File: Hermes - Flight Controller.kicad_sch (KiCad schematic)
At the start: 1 part

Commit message: connector
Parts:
- added R?: (no value), symbol Device:R_Small
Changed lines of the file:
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@@
 (kicad_sch (version 20211123) (generator eeschema)
   (paper "A4")
+  (symbol (lib_id "Device:R_Small") (at 128.27 48.26 0) (unit 1)
+    (in_bom yes) (on_board yes) (fields_autoplaced)
+    (property "Reference" "R?" (id 0) (at 130.81 46.9899 0)
+      (effects (font (size 1.27 1.27)) (justify left))
+    )
+    (property "Value" "" (id 1) (at 130.81 49.5299 0)
+      (effects (font (size 1.27 1.27)) (justify left))
+    )
+    (property "Footprint" "" (id 2) (at 128.27 48.26 0)
+      (effects (font (size 1.27 1.27)) hide)
+    )
+    (property "Datasheet" "~" (id 3) (at 128.27 48.26 0)
+      (effects (font (size 1.27 1.27)) hide)
+    )
+    (pin "1")
+    (pin "2")
+  )
   (symbol (lib_id "Connector:USB_C_Receptacle_USB2.0") (at 88.9 54.61 0) (unit 1)
     (in_bom yes) (on_board yes) (fields_autoplaced)
@@
       (reference "J?") (unit 1) (value "USB_C_Receptacle_USB2.0") (footprint "")
     )
+    (path "/d8f1aa4a-2f21-4570-b6e4-a5df899c3581"
+      (reference "R?") (unit 1) (value "R_Small") (footprint "")
+    )
   )

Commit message: usbc implementation
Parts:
- added C? (x2): (no value), symbol Device:C_Small
- added FB?: (no value), symbol Device:FerriteBead_Small
- added R?: 5.1k, Resistor_SMD:R_0603_1608Metric_Pad0.98x0.95mm_HandSolder, symbol Device:R_Small
- added U?: USBLC6-2SC6, SnapEDA Library:SOT95P280X145-6N, symbol USBLC6-2SC6:USBLC6-2SC6
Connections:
- net at R?.1: now also J?.B5 (CC2)
- net GND: now reaches R?.2
- net GND: now also J?.A1 (GND), J?.A12 (GND), J?.B1 (GND), J?.B12 (GND), C?.2, C?.2, R?.2, U?.2
- net VBUS: now reaches J?.A4 (VBUS), J?.A9 (VBUS), J?.B4 (VBUS), J?.B9 (VBUS)
- net VBUS: now also C?.1, FB?.1, U?.5
- net at J?.A5 (CC1): now also R?.1
- net USB_CON_D+: now reaches J?.A6 (D+)
- net USB_CON_D+: now also J?.B6 (D+), U?.1
- net USB_CON_D-: now reaches J?.A7 (D-)
- net USB_CON_D-: now also J?.B7 (D-), U?.3
- new net: C?.1, FB?.2
- new net USB_D+: U?.6
- new net USB_D-: U?.4
- no-connect marks 0 -> 3
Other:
- moved on the sheet: R?

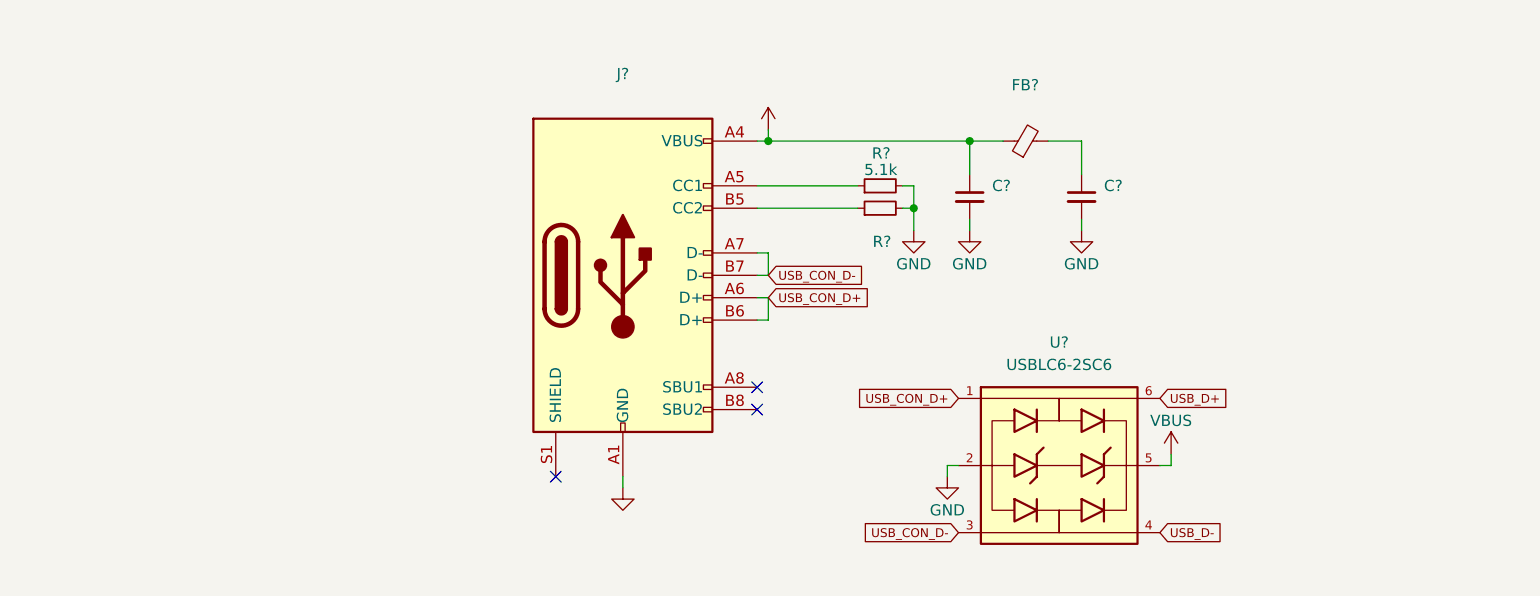
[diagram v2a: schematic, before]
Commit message: added battery charge circuit
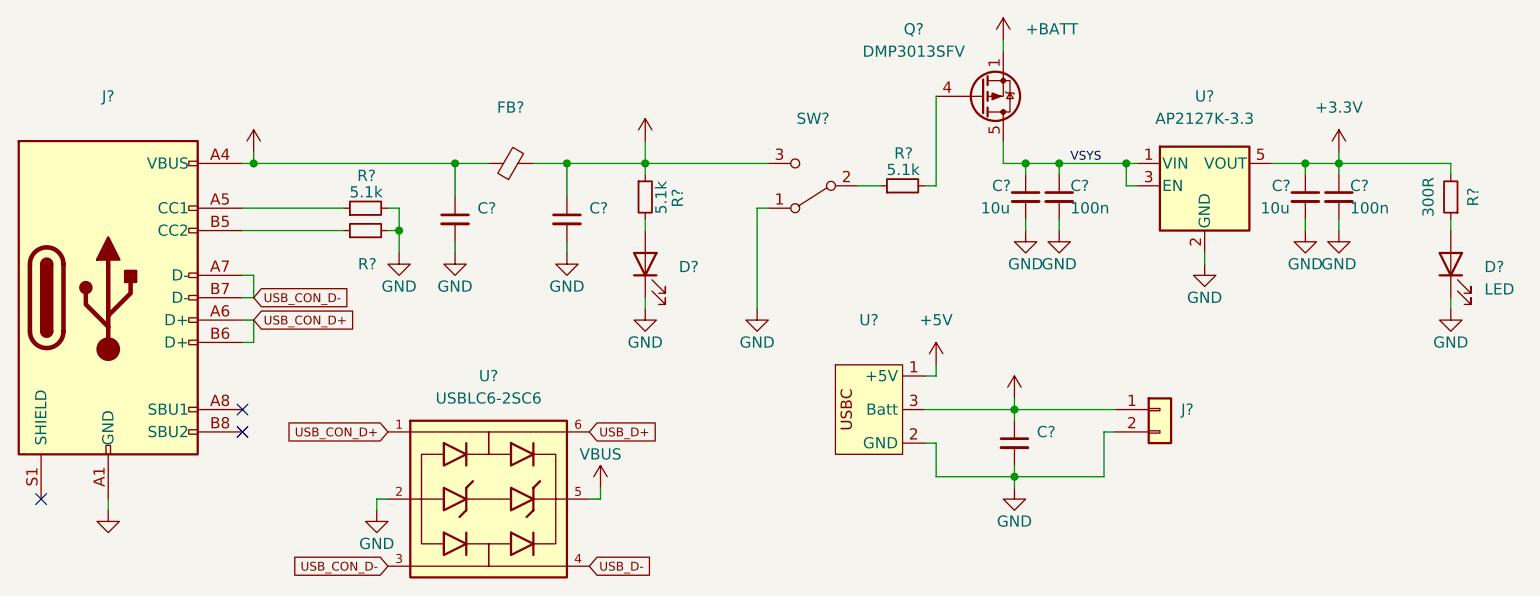
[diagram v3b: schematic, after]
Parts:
- added C?: (no value), symbol Device:C_Small
- added C? (x2): 10u, Resistor_SMD:R_0603_1608Metric_Pad0.98x0.95mm_HandSolder, symbol Device:C_Small
- added C? (x2): 100n, Resistor_SMD:R_0603_1608Metric_Pad0.98x0.95mm_HandSolder, symbol Device:C_Small
- added D?: LED, Resistor_SMD:R_0603_1608Metric_Pad0.98x0.95mm_HandSolder, symbol Device:LED
- added D?: (no value), symbol Device:LED
- added J?: (no value), symbol Connector_Generic:Conn_01x02
- added Q?: DMP3013SFV, Package_SON:Diodes_PowerDI3333-8, symbol Transistor_FET:DMP3013SFV
- added R? (x2): 5.1k, Resistor_SMD:R_0603_1608Metric_Pad0.98x0.95mm_HandSolder, symbol Device:R_Small
- added R?: 300R, Resistor_SMD:R_0603_1608Metric_Pad0.98x0.95mm_HandSolder, symbol Device:R_Small
- added SW?: (no value), symbol Switch:SW_SPDT
- added U?: AP2127K-3.3, Package_TO_SOT_SMD:SOT-23-5, symbol Regulator_Linear:AP2127K-3.3
- added U?: (no value), symbol usbc_batt:usbc_batt
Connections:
- net GND: now also C?.2, C?.2, C?.2, C?.2, C?.2, D?.1 (K), D?.1 (K), J?.2 (Pin_2), SW?.1 (A), U?.2 (GND), U?.2 (GND)
- net +5V: now reaches C?.1, FB?.2
- net +5V: now also R?.1, SW?.3 (C), U?.1 (+5V)
- new net: R?.1, SW?.2 (B)
- new net: D?.2 (A), R?.1
- new net: D?.2 (A), R?.2
- new net: Q?.4 (G), R?.2
- new net +3V3: C?.1, C?.1, R?.2, U?.5 (VOUT)
- new net +BATT: C?.1, J?.1 (Pin_1), Q?.1 (S), Q?.2 (S), Q?.3 (S), U?.3 (Batt)
- new net VSYS: C?.1, C?.1, Q?.5 (D), U?.1 (VIN), U?.3 (EN)
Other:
- moved on the sheet: C?, FB?, J?, R?, U?

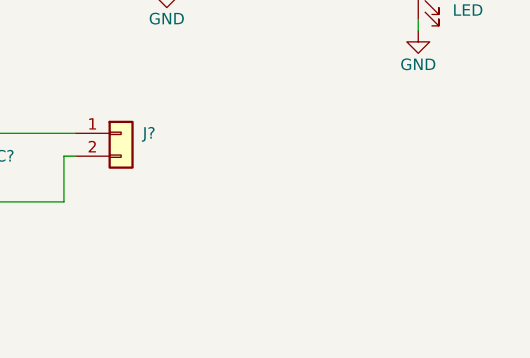
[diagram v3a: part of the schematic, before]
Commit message: opting for 2S battery config
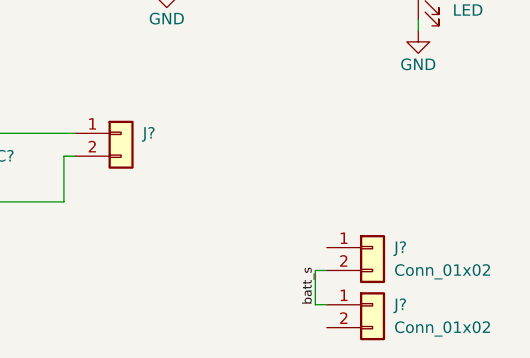
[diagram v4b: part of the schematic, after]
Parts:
- added J? (x2): Conn_01x02, symbol Connector_Generic:Conn_01x02
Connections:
- new net batt_s: J?.1 (Pin_1), J?.2 (Pin_2)
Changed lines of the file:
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@@
+    (stroke (width 0) (type default) (color 0 0 0 0))
+  )
+  (wire (pts (xy 172.72 85.09) (xy 171.45 85.09))
     (stroke (width 0) (type default) (color 0 0 0 0))
   )
@@
     (stroke (width 0) (type default) (color 0 0 0 0))
   )
+  (wire (pts (xy 171.45 85.09) (xy 171.45 88.9))
+    (stroke (width 0) (type default) (color 0 0 0 0))
+  )
   (wire (pts (xy 133.35 76.2) (xy 133.35 77.47))
     (stroke (width 0) (type default) (color 0 0 0 0))
@@
     (stroke (width 0) (type default) (color 0 0 0 0))
   )
+  (wire (pts (xy 171.45 88.9) (xy 172.72 88.9))
+    (stroke (width 0) (type default) (color 0 0 0 0))
+  )
   (label "VSYS" (at 139.7 41.91 0)
+    (effects (font (size 1 1)) (justify left bottom))
+  )
+  (label "batt_s" (at 171.45 88.9 90)
     (effects (font (size 1 1)) (justify left bottom))
   )
@@
     )
     (property "Datasheet" "~" (id 3) (at 182.88 45.72 0)
+      (effects (font (size 1.27 1.27)) hide)
+    )
+    (pin "1")
+    (pin "2")
+  )
+  (symbol (lib_id "Connector_Generic:Conn_01x02") (at 177.8 82.55 0) (unit 1)
+    (in_bom yes) (on_board yes) (fields_autoplaced)
+    (property "Reference" "J?" (id 0) (at 180.2029 82.5499 0)
+      (effects (font (size 1.27 1.27)) (justify left))
+    )
+    (property "Value" "Conn_01x02" (id 1) (at 180.2029 85.0899 0)
+      (effects (font (size 1.27 1.27)) (justify left))
+    )
+    (property "Footprint" "" (id 2) (at 177.8 82.55 0)
+      (effects (font (size 1.27 1.27)) hide)
+    )
+    (property "Datasheet" "~" (id 3) (at 177.8 82.55 0)
       (effects (font (size 1.27 1.27)) hide)
     )
@@
     (pin "2")
   )
+  (symbol (lib_id "Connector_Generic:Conn_01x02") (at 177.8 88.9 0) (unit 1)
+    (in_bom yes) (on_board yes) (fields_autoplaced)
+    (property "Reference" "J?" (id 0) (at 180.2029 88.8999 0)
+      (effects (font (size 1.27 1.27)) (justify left))
+    )
+    (property "Value" "Conn_01x02" (id 1) (at 180.2029 91.4399 0)
+      (effects (font (size 1.27 1.27)) (justify left))
+    )
+    (property "Footprint" "" (id 2) (at 177.8 88.9 0)
+      (effects (font (size 1.27 1.27)) hide)
+    )
+    (property "Datasheet" "~" (id 3) (at 177.8 88.9 0)
+      (effects (font (size 1.27 1.27)) hide)
+    )
+    (pin "1")
+    (pin "2")
+  )
   (sheet_instances
     (path "/" (page "1"))
@@
       (reference "J?") (unit 1) (value "Conn_01x02") (footprint "")
     )
+    (path "/bf5d4925-6bbb-4b21-ad5f-088d9d96ac60"
+      (reference "J?") (unit 1) (value "Conn_01x02") (footprint "")
+    )
     (path "/f12d2856-5cdd-423a-969e-209ea0a827b0"
       (reference "J?") (unit 1) (value "USB_C_Receptacle_USB2.0") (footprint "")
     )
+    (path "/fa5a923f-23c4-47c4-bacb-24bf6763083d"
+      (reference "J?") (unit 1) (value "Conn_01x02") (footprint "")
+    )
     (path "/d35736f0-de68-454d-9fb0-1a81541e123d"

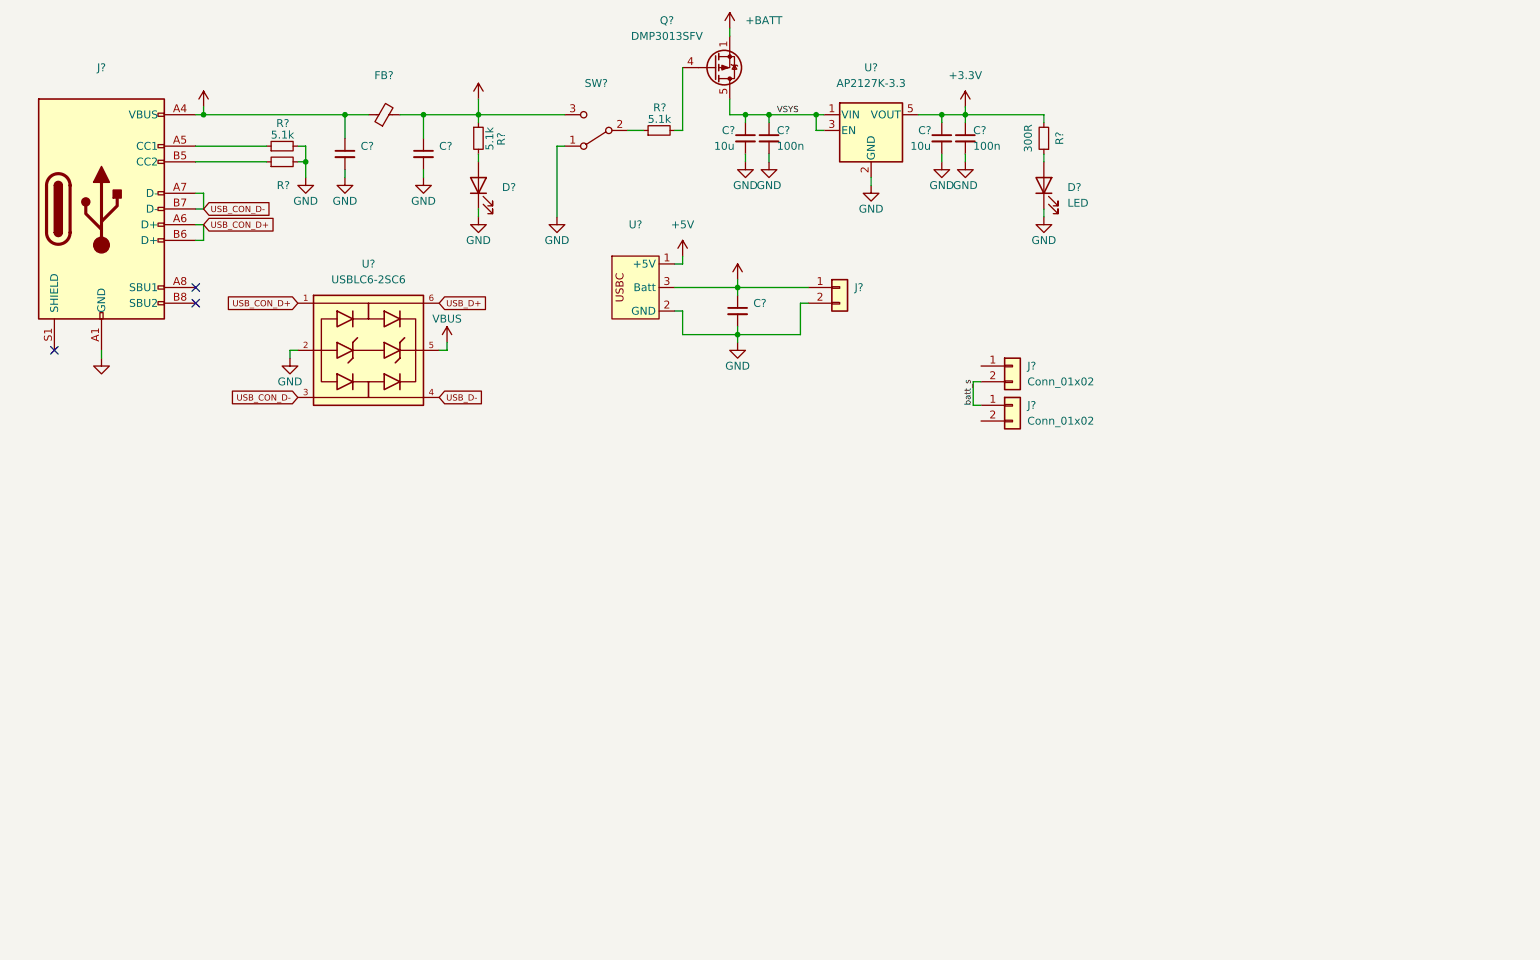
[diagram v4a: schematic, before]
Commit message: added pmic
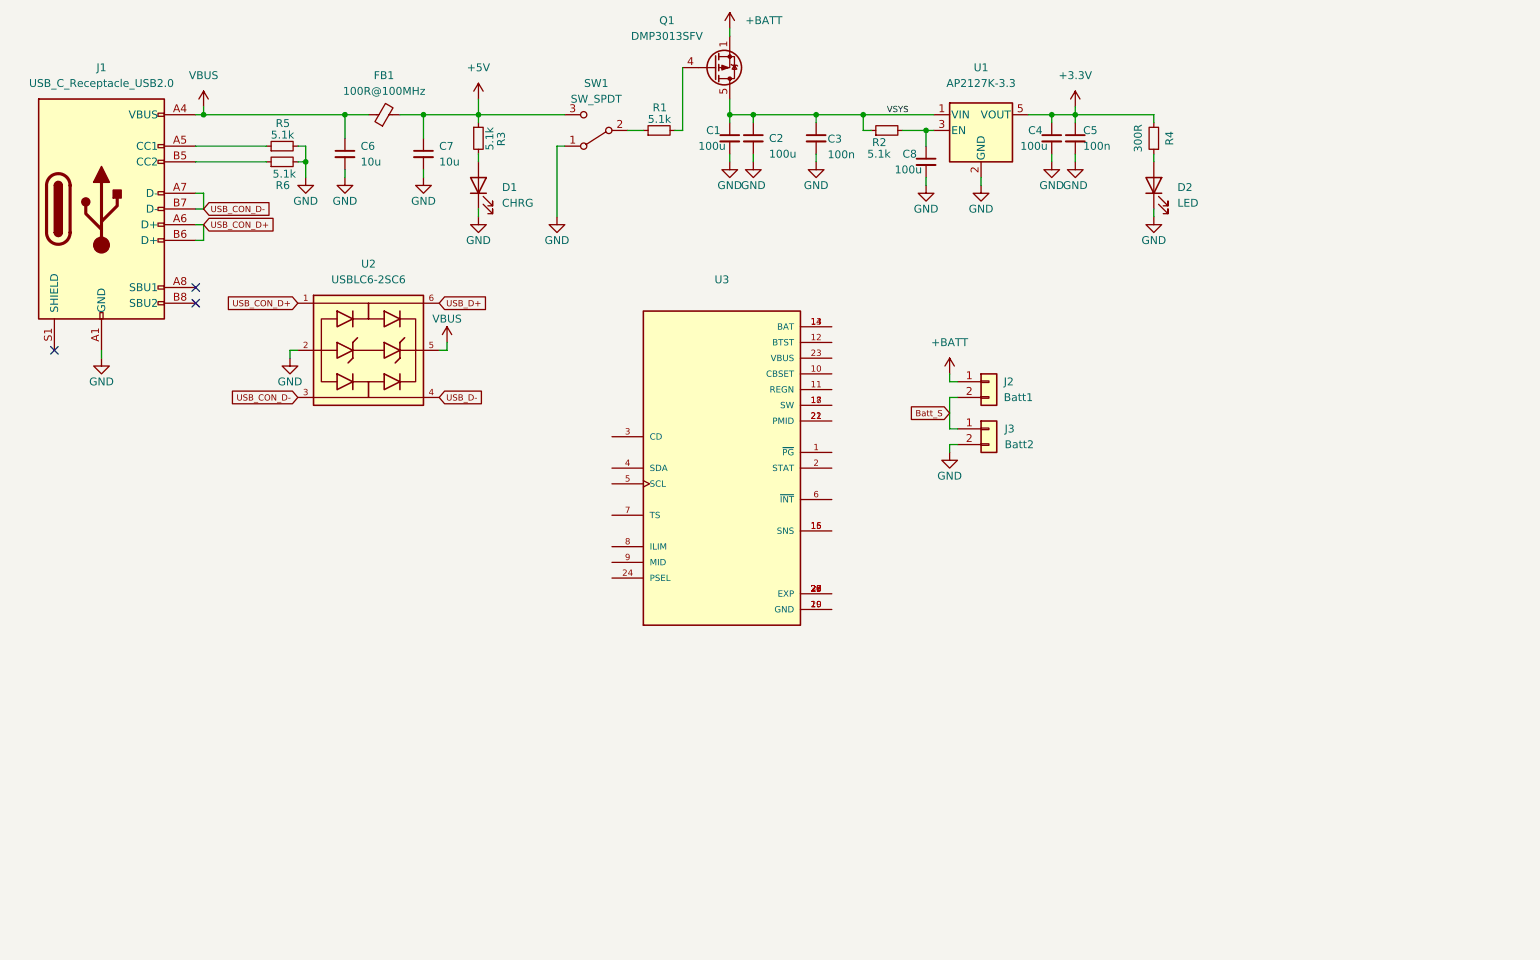
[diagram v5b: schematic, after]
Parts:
- removed C?: (no value), symbol Device:C_Small
- removed J?: (no value), symbol Connector_Generic:Conn_01x02
- removed U?: (no value), symbol usbc_batt:usbc_batt
- added C3: 100n, Resistor_SMD:R_0603_1608Metric_Pad0.98x0.95mm_HandSolder, symbol Device:C_Small
- added C8: 100u, Resistor_SMD:R_0805_2012Metric_Pad1.20x1.40mm_HandSolder, symbol Device:C_Small
- added R2: 5.1k, Resistor_SMD:R_0603_1608Metric_Pad0.98x0.95mm_HandSolder, symbol Device:R_Small
- added U3: (no value), symbol BQ25887RGER:BQ25887RGER
- C1, C4: renamed from C?; value 10u -> 100u; footprint Resistor_SMD:R_0603_1608Metric_Pad0.98x0.95mm_HandSolder -> Resistor_SMD:R_0805_2012Metric_Pad1.20x1.40mm_HandSolder
- C2: renamed from C?; value 100n -> 100u; footprint Resistor_SMD:R_0603_1608Metric_Pad0.98x0.95mm_HandSolder -> Resistor_SMD:R_0805_2012Metric_Pad1.20x1.40mm_HandSolder
- C6, C7: renamed from C?; value (none) -> 10u; footprint (none) -> Capacitor_SMD:C_0603_1608Metric_Pad1.08x0.95mm_HandSolder
- D1: renamed from D?; value (none) -> CHRG; footprint (none) -> LED_SMD:LED_0603_1608Metric_Pad1.05x0.95mm_HandSolder
- FB1: renamed from FB?; value (none) -> 100R@100MHz; footprint (none) -> Resistor_SMD:R_0603_1608Metric_Pad0.98x0.95mm_HandSolder
- J1: renamed from J?; value (none) -> USB_C_Receptacle_USB2.0
- J2: renamed from J?; value Conn_01x02 -> Batt1
- J3: renamed from J?; value Conn_01x02 -> Batt2
- R6: renamed from R?; value (none) -> 5.1k; footprint (none) -> Resistor_SMD:R_0603_1608Metric_Pad0.98x0.95mm_HandSolder
- SW1: renamed from SW?; value (none) -> SW_SPDT
- gave numbers to parts that had none: 9
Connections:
- net +BATT: now also J2.1 (Pin_1)
- net GND: now also J3.2 (Pin_2), C3.2, C8.2
- net VSYS: now also C3.1, R2.1; no longer U1.3 (EN)
- net batt_s renamed Batt_S
- new net: C8.1, R2.2, U1.3 (EN)
- new net: U3.13 (BAT), U3.14 (BAT)
- new net: U3.15 (SNS), U3.16 (SNS)
- new net: U3.17 (SW), U3.18 (SW)
- new net: U3.19 (GND), U3.20 (GND)
- new net: U3.21 (PMID), U3.22 (PMID)
- new net: U3.25 (EXP), U3.26 (EXP), U3.27 (EXP), U3.28 (EXP), U3.29 (EXP), U3.30 (EXP)
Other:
- moved on the sheet: C1, C2, C4, C5, D2, J2, J3, R4, U1

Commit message: battery mngmt
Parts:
- added C?: 10u, Capacitor_SMD:C_0603_1608Metric_Pad1.08x0.95mm_HandSolder, symbol Device:C_Small
- added L?: (no value), symbol Device:L_Small
- added R?: 5.1k, Resistor_SMD:R_0603_1608Metric_Pad0.98x0.95mm_HandSolder, symbol Device:R_Small
- U3: value (none) -> BQ25887RGER; footprint (none) -> SnapEDA Library:IC_BQ25887RGER
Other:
- moved on the sheet: J2, J3, U3
